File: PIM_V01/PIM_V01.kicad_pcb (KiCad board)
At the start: 2 copper layers, 95.9 x 90.2 mm, 10 parts, among them J1 Conn_02x30_Row_Letter_First, J2 Conn_02x30_Row_Letter_First

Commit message: a month of progress, schematic is nearly done (just needs to be checked), and layout is getting close'
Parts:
- removed H1, H2, H3, H4: MountingHole_Pad, MountingHole:MountingHole_3.2mm_M3_Pad_TopBottom
- removed H5, H6, H7, H8: MountingHole, MountingHole:MountingHole_2mm
- removed J2: Conn_02x30_Row_Letter_First, Connector_PinSocket_2.00mm:PinSocket_2x30_P2.00mm_Vertical
- added C1: 1uF, Capacitor_SMD:C_0603_1608Metric, F.Cu at (466.8, 68.0)
- added C10: 4.7uF, Capacitor_SMD:C_0603_1608Metric, F.Cu at (484.0, 103.5)
- added C100: 27pF, Capacitor_SMD:C_0603_1608Metric, F.Cu at (511.4, 136.0)
- added C101: 22uF, Capacitor_SMD:C_0603_1608Metric, F.Cu at (554.0, 70.8)
- added C102: 22uF, Capacitor_SMD:C_0603_1608Metric, F.Cu at (555.5, 70.8)
- added C11: 4.7uF, Capacitor_SMD:C_0603_1608Metric, F.Cu at (483.5, 115.5)
- added C12: 0.1uF, Capacitor_SMD:C_0603_1608Metric, F.Cu at (482.5, 103.5)
- added C13: 0.1uF, Capacitor_SMD:C_0603_1608Metric, F.Cu at (482.0, 115.5)
- added C14: 4.7uF, Capacitor_SMD:C_0603_1608Metric, F.Cu at (476.5, 99.2)
- added C15: 4.7uF, Capacitor_SMD:C_0603_1608Metric, F.Cu at (476.5, 111.2)
- added C16: 0.1uF, Capacitor_SMD:C_0603_1608Metric, F.Cu at (475.0, 99.2)
- added C17: 0.1uF, Capacitor_SMD:C_0603_1608Metric, F.Cu at (475.0, 111.2)
- added C18: 47pF, Capacitor_SMD:C_0603_1608Metric, F.Cu at (465.5, 102.0)
- added C19: 47pF, Capacitor_SMD:C_0603_1608Metric, F.Cu at (465.5, 114.0)
- added C2: 0.1uF, Capacitor_SMD:C_0603_1608Metric, F.Cu at (468.3, 68.0)
- added C20: 47pF, Capacitor_SMD:C_0603_1608Metric, F.Cu at (465.5, 105.0)
- added C21: 47pF, Capacitor_SMD:C_0603_1608Metric, F.Cu at (465.5, 117.0)
- added C22: 47pF, Capacitor_SMD:C_0603_1608Metric, F.Cu at (455.0, 102.0)
- added C23: 47pF, Capacitor_SMD:C_0603_1608Metric, F.Cu at (455.0, 114.0)
- added C24: 47pF, Capacitor_SMD:C_0603_1608Metric, F.Cu at (455.0, 105.0)
- added C25: 47pF, Capacitor_SMD:C_0603_1608Metric, F.Cu at (455.0, 117.0)
- added C26: 4.7nF, Capacitor_SMD:C_0603_1608Metric, F.Cu at (462.0, 106.5)
- added C27: 4.7nF, Capacitor_SMD:C_0603_1608Metric, F.Cu at (462.0, 118.5)
- added C28: 10uF, Capacitor_SMD:C_0603_1608Metric, F.Cu at (502.2, 67.1)
- added C29: 10uF, Capacitor_SMD:C_0603_1608Metric, F.Cu at (484.2, 67.2)
- added C3: 3.3nF, Capacitor_SMD:C_0603_1608Metric, F.Cu at (469.8, 63.4)
- added C30: 10uF, Capacitor_SMD:C_0603_1608Metric, F.Cu at (519.0, 67.0)
- added C31: 10uF, Capacitor_SMD:C_0603_1608Metric, F.Cu at (503.7, 67.1)
- added C32: 10uF, Capacitor_SMD:C_0603_1608Metric, F.Cu at (485.7, 67.2)
- added C33: 10uF, Capacitor_SMD:C_0603_1608Metric, F.Cu at (520.5, 67.0)
- added C34: 0.1uF, Capacitor_SMD:C_0603_1608Metric, F.Cu at (505.2, 67.1)
- added C35: 0.1uF, Capacitor_SMD:C_0603_1608Metric, F.Cu at (487.2, 67.2)
- added C36: 0.1uF, Capacitor_SMD:C_0603_1608Metric, F.Cu at (522.0, 67.0)
- added C37: 33nF, Capacitor_SMD:C_0603_1608Metric, F.Cu at (510.9, 65.0)
- added C38: 10nF, Capacitor_SMD:C_0603_1608Metric, F.Cu at (492.7, 65.1)
- added C39: 33nF, Capacitor_SMD:C_0603_1608Metric, F.Cu at (527.5, 65.0)
- added C4: 47uF, Capacitor_SMD:C_0603_1608Metric, F.Cu at (448.5, 67.5)
- added C40: 0.1uF, Capacitor_SMD:C_0603_1608Metric, F.Cu at (514.4, 66.5)
- added C41: 0.1uF, Capacitor_SMD:C_0603_1608Metric, F.Cu at (496.4, 66.6)
- added C42: 0.1uF, Capacitor_SMD:C_0603_1608Metric, F.Cu at (531.0, 66.5)
- added C43: 22uF, Capacitor_SMD:C_0603_1608Metric, F.Cu at (507.3, 79.1)
- added C44: 22uF, Capacitor_SMD:C_0603_1608Metric, F.Cu at (489.2, 79.1)
- added C45: 22uF, Capacitor_SMD:C_0603_1608Metric, F.Cu at (524.0, 78.8)
- added C46: 22uF, Capacitor_SMD:C_0603_1608Metric, F.Cu at (507.3, 80.6)
- added C47: 22uF, Capacitor_SMD:C_0603_1608Metric, F.Cu at (489.2, 80.6)
- added C48: 22uF, Capacitor_SMD:C_0603_1608Metric, F.Cu at (524.0, 80.3)
- added C49: 10uF, Capacitor_SMD:C_0603_1608Metric, F.Cu at (549.0, 93.9)
- added C5: 47uF, Capacitor_SMD:C_0603_1608Metric, F.Cu at (450.0, 67.5)
- added C50: 10uF, Capacitor_SMD:C_0603_1608Metric, F.Cu at (549.2, 111.0)
- added C51: 10uF, Capacitor_SMD:C_0603_1608Metric, F.Cu at (549.0, 92.4)
- added C52: 10uF, Capacitor_SMD:C_0603_1608Metric, F.Cu at (549.2, 109.5)
- added C53: 0.1uF, Capacitor_SMD:C_0603_1608Metric, F.Cu at (549.0, 90.9)
- added C54: 0.1uF, Capacitor_SMD:C_0603_1608Metric, F.Cu at (549.2, 108.0)
- added C55: 10nF, Capacitor_SMD:C_0603_1608Metric, F.Cu at (546.9, 85.4)
- added C56: 10nF, Capacitor_SMD:C_0603_1608Metric, F.Cu at (546.9, 102.3)
- added C57: 0.1uF, Capacitor_SMD:C_0603_1608Metric, F.Cu at (548.4, 82.0)
- added C58: 0.1uF, Capacitor_SMD:C_0603_1608Metric, F.Cu at (548.4, 98.8)
- added C59: 22uF, Capacitor_SMD:C_0603_1608Metric, F.Cu at (561.4, 89.1)
- added C6: 10uF, Capacitor_SMD:C_0603_1608Metric, F.Cu at (451.5, 67.5)
- added C60: 22uF, Capacitor_SMD:C_0603_1608Metric, F.Cu at (561.3, 106.0)
- added C61: 22uF, Capacitor_SMD:C_0603_1608Metric, F.Cu at (562.9, 89.1)
- added C62: 22uF, Capacitor_SMD:C_0603_1608Metric, F.Cu at (562.8, 106.0)
- added C63: 100nF, Capacitor_SMD:C_0603_1608Metric, F.Cu at (524.0, 100.5)
- added C64: 27pF, Capacitor_SMD:C_0603_1608Metric, F.Cu at (530.7, 141.0)
- added C65: 10nF, Capacitor_SMD:C_0603_1608Metric, F.Cu at (504.0, 64.3)
- added C66: 10nF, Capacitor_SMD:C_0603_1608Metric, F.Cu at (486.0, 64.5)
- added C67: 10nF, Capacitor_SMD:C_0603_1608Metric, F.Cu at (520.7, 64.4)
- added C68: 100uF, Capacitor_SMD:C_0603_1608Metric, F.Cu at (539.5, 71.1)
- added C69: 22uF, Capacitor_SMD:C_0603_1608Metric, F.Cu at (541.0, 71.1)
- added C7: 10uF, Capacitor_SMD:C_0603_1608Metric, F.Cu at (445.0, 86.7)
- added C70: 0.1uF, Capacitor_SMD:C_0603_1608Metric, F.Cu at (542.5, 71.1)
- added C71: 22nF, Capacitor_SMD:C_0603_1608Metric, F.Cu at (546.0, 76.6)
- added C72: 1uF, Capacitor_SMD:C_0603_1608Metric, F.Cu at (550.0, 73.6)
- added C73: 0.1uF, Capacitor_SMD:C_0603_1608Metric, F.Cu at (541.2, 67.4)
- added C74: 0.1uF, Capacitor_SMD:C_0603_1608Metric, F.Cu at (551.7, 67.4)
- added C75: 100uF, Capacitor_SMD:C_0603_1608Metric, F.Cu at (557.0, 70.8)
- added C76: 22uF, Capacitor_SMD:C_0603_1608Metric, F.Cu at (552.5, 70.8)
- added C77: 22uF, Capacitor_SMD:C_0603_1608Metric, F.Cu at (551.0, 70.8)
- added C78: 1uF, Capacitor_SMD:C_0603_1608Metric, F.Cu at (448.8, 80.2)
- added C79: 1uF, Capacitor_SMD:C_0603_1608Metric, F.Cu at (454.8, 80.2)
- added C8: 1uF, Capacitor_SMD:C_0603_1608Metric, F.Cu at (475.4, 68.3)
- added C80: 1uF, Capacitor_SMD:C_0603_1608Metric, F.Cu at (500.1, 86.3)
- added C81: 0.1uF, Capacitor_SMD:C_0603_1608Metric, F.Cu at (498.6, 86.3)
- added C82: 10uF, Capacitor_SMD:C_0603_1608Metric, F.Cu at (445.0, 80.3)
- added C83: 0.1uF, Capacitor_SMD:C_0603_1608Metric, F.Cu at (507.3, 77.6)
- added C84: 0.1uF, Capacitor_SMD:C_0603_1608Metric, F.Cu at (489.2, 77.6)
- added C85: 0.1uF, Capacitor_SMD:C_0603_1608Metric, F.Cu at (524.0, 77.3)
- added C86: 0.1uF, Capacitor_SMD:C_0603_1608Metric, F.Cu at (559.9, 89.1)
- added C87: 0.1uF, Capacitor_SMD:C_0603_1608Metric, F.Cu at (559.8, 106.0)
- added C88: 0.1uF, Capacitor_SMD:C_0603_1608Metric, F.Cu at (549.5, 70.8)
- added C89: 0.1uF, Capacitor_SMD:C_0603_1608Metric, F.Cu at (500.8, 108.0)
- added C9: 10uF, Capacitor_SMD:C_0603_1608Metric, F.Cu at (469.1, 79.5)
- added C90: 0.1uF, Capacitor_SMD:C_0603_1608Metric, F.Cu at (517.5, 111.0)
- added C91: 0.1uF, Capacitor_SMD:C_0603_1608Metric, F.Cu at (520.0, 105.4)
- added C92: 0.1uF, Capacitor_SMD:C_0603_1608Metric, F.Cu at (520.0, 102.3)
- added C93: 0.1uF, Capacitor_SMD:C_0603_1608Metric, F.Cu at (503.7, 91.5)
- added C94: 4.7uF, Capacitor_SMD:C_0603_1608Metric, F.Cu at (516.8, 91.3)
- added C95: 1uF, Capacitor_SMD:C_0603_1608Metric, F.Cu at (520.5, 96.5)
- added C96: 2.2uF, Capacitor_SMD:C_0603_1608Metric, F.Cu at (503.0, 88.5)
- added C97: 2.2uF, Capacitor_SMD:C_0603_1608Metric, F.Cu at (498.5, 106.3)
- added C98: 0.1uF, Capacitor_SMD:C_0603_1608Metric, F.Cu at (522.0, 96.5)
- added C99: 1uF, Capacitor_SMD:C_0603_1608Metric, F.Cu at (523.5, 96.5)
- added D1: SMBJ13A, CustomFootprints:SMBJ16A, F.Cu at (445.5, 67.5)
- added D10: LED, LED_SMD:LED_0603_1608Metric, F.Cu at (486.2, 82.1)
- added D11: LED, LED_SMD:LED_0603_1608Metric, F.Cu at (568.0, 86.4)
- added D12: LED, LED_SMD:LED_0603_1608Metric, F.Cu at (568.2, 102.9)
- added D13: SMAJ13A, Diode_SMD:D_SMA, F.Cu at (464.0, 65.9)
- added D2: LED, LED_SMD:LED_0603_1608Metric, F.Cu at (439.8, 91.5)
- added D3: PMEG4010, Diode_SMD:Nexperia_CFP3_SOD-123W, F.Cu at (473.5, 69.1)
- added D4: BZT52C15, Diode_SMD:Nexperia_CFP3_SOD-123W, F.Cu at (461.0, 66.5)
- added D5: D_TVS_Dual_AAC, Package_TO_SOT_SMD:SOT-23-3, F.Cu at (468.5, 115.5)
- added D6: D_TVS_Dual_AAC, Package_TO_SOT_SMD:SOT-23-3, F.Cu at (468.5, 103.5)
- added D7: D_TVS_Dual_AAC, Package_TO_SOT_SMD:SOT-23-3, F.Cu at (450.5, 103.5)
- added D8: D_TVS_Dual_AAC, Package_TO_SOT_SMD:SOT-23-3, F.Cu at (450.5, 115.5)
- added D9: LED, LED_SMD:LED_0603_1608Metric, F.Cu at (504.2, 82.2)
- added FL1: Choke_CommonMode_FerriteCore_1243, Inductor_SMD:L_CommonModeChoke_Coilcraft_1812CAN, F.Cu at (462.0, 103.5)
- added FL2: Choke_CommonMode_FerriteCore_1243, Inductor_SMD:L_CommonModeChoke_Coilcraft_1812CAN, F.Cu at (462.0, 115.5)
- added J10: Conn_02x08_Odd_Even, Connector_PinHeader_2.54mm:PinHeader_2x08_P2.54mm_Vertical, F.Cu at (525.7, 123.0)
- added J11: Conn_01x02, Connector_PinHeader_2.54mm:PinHeader_1x02_P2.54mm_Vertical, F.Cu at (563.7, 83.3)
- added J12: Conn_01x02, Connector_PinHeader_2.54mm:PinHeader_1x02_P2.54mm_Vertical, F.Cu at (563.9, 100.0)
- added J13: Conn_01x02, Connector_PinHeader_2.54mm:PinHeader_1x02_P2.54mm_Vertical, F.Cu at (563.7, 70.3)
- added J4: USB_C_Receptacle_USB2.0_14P, Connector_USB:USB_C_Receptacle_HCTL_HC-TYPE-C-16P-01A, F.Cu at (439.3, 83.5)
- added J5: Conn_01x04, Connector_Molex:Molex_PicoBlade_53261-0471_1x04-1MP_P1.25mm_Horizontal, F.Cu at (438.5, 103.5)
- added J6: Conn_01x04, Connector_Molex:Molex_PicoBlade_53261-0471_1x04-1MP_P1.25mm_Horizontal, F.Cu at (438.5, 115.5)
- added J7: Conn_02x03_Odd_Even, Connector_PinHeader_2.54mm:PinHeader_2x03_P2.54mm_Vertical, F.Cu at (495.0, 115.3)
- added J8: Conn_01x02, Connector_PinHeader_2.54mm:PinHeader_1x02_P2.54mm_Vertical, F.Cu at (513.5, 118.0)
- added J9: Conn_02x08_Odd_Even, Connector_PinHeader_2.54mm:PinHeader_2x08_P2.54mm_Vertical, F.Cu at (504.0, 123.0)
- added L1: 6.8uH, CustomFootprints:L_Wurth_WE-LHMI-7030, F.Cu at (511.0, 72.4)
- added L2: 6.8uH, CustomFootprints:L_Wurth_WE-LHMI-7030, F.Cu at (492.5, 72.4)
- added L3: 6.8uH, CustomFootprints:L_Wurth_WE-LHMI-7030, F.Cu at (527.0, 72.0)
- added L4: 6.8uH, CustomFootprints:L_Wurth_WE-LHMI-7030, F.Cu at (554.0, 85.4)
- added L5: 6.8uH, CustomFootprints:L_Wurth_WE-LHMI-7030, F.Cu at (554.0, 102.5)
- added L6: 4.7uH, CustomFootprints:L_Wurth_WE-LHMI-7050, F.Cu at (546.5, 63.5)
- added Q1: SQJ407EP-T1_GE3, CustomFootprints:PowerPAK-SO-8L_Option-2_VIS, F.Cu at (456.0, 67.5)
- added Q2: PMOS, Package_TO_SOT_SMD:SOT-23-3, F.Cu at (472.1, 77.5)
- added Q3: PMOS, Package_TO_SOT_SMD:SOT-23-3, F.Cu at (472.1, 81.5)
- added Q4: NMOS, Package_TO_SOT_SMD:SOT-23-3, F.Cu at (472.1, 73.5)
- added R1: 5k1R, Resistor_SMD:R_0603_1608Metric, F.Cu at (442.7, 77.3)
- added R10: 0R, Resistor_SMD:R_0603_1608Metric, F.Cu at (549.5, 68.1)
- added R11: 0R, Resistor_SMD:R_0603_1608Metric, F.Cu at (475.1, 79.2)
- added R12: 1MR, Resistor_SMD:R_0603_1608Metric, F.Cu at (476.6, 79.2)
- added R13: 10kR, Resistor_SMD:R_0603_1608Metric, F.Cu at (512.7, 115.4)
- added R14: 10kR, Resistor_SMD:R_0603_1608Metric, F.Cu at (475.8, 109.0)
- added R15: 10kR, Resistor_SMD:R_0603_1608Metric, F.Cu at (476.0, 121.0)
- added R16: 0R, Resistor_SMD:R_0603_1608Metric, F.Cu at (475.8, 107.5)
- added R17: 0R, Resistor_SMD:R_0603_1608Metric, F.Cu at (476.0, 119.5)
- added R18: 60R, Resistor_SMD:R_0603_1608Metric, F.Cu at (453.5, 105.0)
- added R19: 60R, Resistor_SMD:R_0603_1608Metric, F.Cu at (453.5, 102.0)
- added R2: 866kR, Resistor_SMD:R_0603_1608Metric, F.Cu at (467.5, 65.7)
- added R20: 60R, Resistor_SMD:R_0603_1608Metric, F.Cu at (453.5, 117.0)
- added R21: 60R, Resistor_SMD:R_0603_1608Metric, F.Cu at (453.5, 114.0)
- added R22: 0R, Resistor_SMD:R_0603_1608Metric, F.Cu at (506.7, 62.0)
- added R23: 0R, Resistor_SMD:R_0603_1608Metric, F.Cu at (488.7, 62.2)
- added R24: 0R, Resistor_SMD:R_0603_1608Metric, F.Cu at (523.5, 62.0)
- added R25: 52.3kR, Resistor_SMD:R_0603_1608Metric, F.Cu at (510.4, 62.0)
- added R26: 10kR, Resistor_SMD:R_0603_1608Metric, F.Cu at (508.8, 62.0)
- added R27: 31.6kR, Resistor_SMD:R_0603_1608Metric, F.Cu at (492.2, 62.2)
- added R28: 10kR, Resistor_SMD:R_0603_1608Metric, F.Cu at (490.7, 62.2)
- added R29: 4.99kR, Resistor_SMD:R_0603_1608Metric, F.Cu at (527.0, 62.0)
- added R3: 150kR, Resistor_SMD:R_0603_1608Metric, F.Cu at (467.5, 64.2)
- added R30: 10kR, Resistor_SMD:R_0603_1608Metric, F.Cu at (525.5, 62.0)
- added R31: 470R, Resistor_SMD:R_0603_1608Metric, F.Cu at (507.2, 82.2)
- added R32: 470R, Resistor_SMD:R_0603_1608Metric, F.Cu at (489.2, 82.1)
- added R33: 470R, Resistor_SMD:R_0603_1608Metric, F.Cu at (565.0, 86.4)
- added R34: 470R, Resistor_SMD:R_0603_1608Metric, F.Cu at (565.2, 102.9)
- added R35: 0R, Resistor_SMD:R_0603_1608Metric, F.Cu at (544.0, 89.7)
- added R36: 0R, Resistor_SMD:R_0603_1608Metric, F.Cu at (544.0, 106.5)
- added R37: 52.3kR, Resistor_SMD:R_0603_1608Metric, F.Cu at (544.0, 86.1)
- added R38: 10kR, Resistor_SMD:R_0603_1608Metric, F.Cu at (544.0, 87.6)
- added R39: 31.6kR, Resistor_SMD:R_0603_1608Metric, F.Cu at (544.0, 103.0)
- added R4: 5k1R, Resistor_SMD:R_0603_1608Metric, F.Cu at (442.7, 89.7)
- added R40: 10kR, Resistor_SMD:R_0603_1608Metric, F.Cu at (544.0, 104.5)
- added R41: 1kR, Resistor_SMD:R_0603_1608Metric, F.Cu at (480.0, 111.2)
- added R42: 1kR, Resistor_SMD:R_0603_1608Metric, F.Cu at (480.0, 119.9)
- added R43: 1kR, Resistor_SMD:R_0603_1608Metric, F.Cu at (480.0, 108.0)
- added R44: 1kR, Resistor_SMD:R_0603_1608Metric, F.Cu at (480.0, 99.0)
- added R45: 470kR, Resistor_SMD:R_0603_1608Metric, F.Cu at (503.2, 62.0)
- added R46: 100kR, Resistor_SMD:R_0603_1608Metric, F.Cu at (504.7, 62.0)
- added R47: 470kR, Resistor_SMD:R_0603_1608Metric, F.Cu at (485.2, 62.2)
- added R48: 100kR, Resistor_SMD:R_0603_1608Metric, F.Cu at (486.7, 62.2)
- added R49: 470kR, Resistor_SMD:R_0603_1608Metric, F.Cu at (520.0, 62.0)
- added R5: 511R, Resistor_SMD:R_0603_1608Metric, F.Cu at (474.5, 64.4)
- added R50: 100kR, Resistor_SMD:R_0603_1608Metric, F.Cu at (521.5, 62.0)
- added R51: 4.7kR, Resistor_SMD:R_0603_1608Metric, F.Cu at (513.0, 113.0)
- added R52: 4.7kR, Resistor_SMD:R_0603_1608Metric, F.Cu at (511.5, 113.0)
- added R53: 430kR, Resistor_SMD:R_0603_1608Metric, F.Cu at (550.0, 76.6)
- added R54: 400kR, Resistor_SMD:R_0603_1608Metric, F.Cu at (550.0, 75.1)
- added R55: 21.5kR, Resistor_SMD:R_0603_1608Metric, F.Cu at (544.5, 76.6)
- added R56: 43.2kR, Resistor_SMD:R_0603_1608Metric, F.Cu at (550.0, 78.1)
- added R57: 4.7kR, Resistor_SMD:R_0603_1608Metric, F.Cu at (507.0, 87.0)
- added R58: 4.7kR, Resistor_SMD:R_0603_1608Metric, F.Cu at (505.5, 87.0)
- added R59: 10kR, Resistor_SMD:R_0603_1608Metric, F.Cu at (506.0, 112.7)
- added R6: 470R, Resistor_SMD:R_0603_1608Metric, F.Cu at (442.8, 91.5)
- added R60: 10kR, Resistor_SMD:R_0603_1608Metric, F.Cu at (511.0, 87.0)
- added R61: 10kR, Resistor_SMD:R_0603_1608Metric, F.Cu at (509.5, 87.0)
- added R62: 33R, Resistor_SMD:R_0603_1608Metric, F.Cu at (515.5, 86.5)
- added R63: 33R, Resistor_SMD:R_0603_1608Metric, F.Cu at (513.5, 86.5)
- added R64: 33R, Resistor_SMD:R_0603_1608Metric, F.Cu at (497.5, 98.0)
- added R65: 33R, Resistor_SMD:R_0603_1608Metric, F.Cu at (497.5, 99.5)
- added R66: 10kR, Resistor_SMD:R_0603_1608Metric, F.Cu at (494.5, 98.0)
- added R67: 10kR, Resistor_SMD:R_0603_1608Metric, F.Cu at (497.5, 101.0)
- added R68: 100kR, Resistor_SMD:R_0603_1608Metric, F.Cu at (476.6, 73.4)
- added R69: 1MR, Resistor_SMD:R_0603_1608Metric, F.Cu at (475.1, 73.4)
- added R7: 10kR, Resistor_SMD:R_0603_1608Metric, F.Cu at (474.5, 65.9)
- added R70: 100kR, Resistor_SMD:R_0603_1608Metric, F.Cu at (469.1, 75.5)
- added R71: 100kR, Resistor_SMD:R_0603_1608Metric, F.Cu at (546.4, 109.3)
- added R72: 100kR, Resistor_SMD:R_0603_1608Metric, F.Cu at (546.0, 92.9)
- added R73: 100kR, Resistor_SMD:R_0603_1608Metric, F.Cu at (541.7, 74.0)
- added R74: 0R, Resistor_SMD:R_0603_1608Metric, F.Cu at (528.0, 66.5)
- added R75: 0R, Resistor_SMD:R_0603_1608Metric, F.Cu at (493.3, 66.6)
- added R76: 0R, Resistor_SMD:R_0603_1608Metric, F.Cu at (511.4, 66.5)
- added R77: 0R, Resistor_SMD:R_0603_1608Metric, F.Cu at (548.4, 85.0)
- added R78: 0R, Resistor_SMD:R_0603_1608Metric, F.Cu at (548.4, 101.8)
- added R8: 100kR, Resistor_SMD:R_0603_1608Metric, F.Cu at (461.0, 62.5)
- added R9: 0R, Resistor_SMD:R_0603_1608Metric, F.Cu at (543.5, 68.1)
- added SW1: SW_Push, Button_Switch_SMD:SW_SPST_B3U-1000P, F.Cu at (541.5, 138.5)
- added TP1: TestPoint, TestPoint:TestPoint_Keystone_5000-5004_Miniature, F.Cu at (471.5, 105.5)
- added TP2: TestPoint, TestPoint:TestPoint_Keystone_5000-5004_Miniature, F.Cu at (471.5, 101.5)
- added TP3: TestPoint, TestPoint:TestPoint_Keystone_5000-5004_Miniature, F.Cu at (471.5, 117.5)
- added TP4: TestPoint, TestPoint:TestPoint_Keystone_5000-5004_Miniature, F.Cu at (471.5, 113.5)
- added TP5: TestPoint, TestPoint:TestPoint_Keystone_5000-5004_Miniature, F.Cu at (457.5, 105.5)
- added TP6: TestPoint, TestPoint:TestPoint_Keystone_5000-5004_Miniature, F.Cu at (457.5, 101.5)
- added TP7: TestPoint, TestPoint:TestPoint_Keystone_5000-5004_Miniature, F.Cu at (457.5, 117.5)
- added TP8: TestPoint, TestPoint:TestPoint_Keystone_5000-5004_Miniature, F.Cu at (457.5, 113.5)
- added U1: TPS259541DSGR, CustomFootprints:DSG0008A, F.Cu at (470.7, 66.6)
- added U10: TPS62933, Package_TO_SOT_SMD:SOT-583-8, F.Cu at (547.7, 105.5)
- added U11: AP2112K-3.3, Package_TO_SOT_SMD:SOT-23-5, F.Cu at (451.8, 80.2)
- added U12: MP28167GQ-A-P, CustomFootprints:QFN-16_MP28167_MNP, F.Cu at (546.5, 71.6)
- added U13: MT29F1G01ABAFDWB-IT_F, Package_SON:WSON-8-1EP_8x6mm_P1.27mm_EP3.4x4.3mm, F.Cu at (493.2, 89.0)
- added U14: MB85RS256B, Package_SO:JEITA_SOIC-8_3.9x4.9mm_P1.27mm, F.Cu at (524.5, 143.1)
- added U2: USBLC6-2SC6, Package_TO_SOT_SMD:SOT-23-6, F.Cu at (448.7, 83.5)
- added U3: STM32H7A3VITx, Package_QFP:LQFP-100_14x14mm_P0.5mm, F.Cu at (510.5, 101.0)
- added U4: MCP2562FDT-E/SN, Package_SO:SOIC-8_3.9x4.9mm_P1.27mm, F.Cu at (477.5, 103.5)
- added U5: MCP2562FDT-E/SN, Package_SO:SOIC-8_3.9x4.9mm_P1.27mm, F.Cu at (477.5, 115.5)
- added U6: TPS62933, Package_TO_SOT_SMD:SOT-583-8, F.Cu at (507.8, 65.6)
- added U7: TPS62933, Package_TO_SOT_SMD:SOT-583-8, F.Cu at (489.7, 65.7)
- added U8: TPS62933, Package_TO_SOT_SMD:SOT-583-8, F.Cu at (524.5, 65.5)
- added U9: TPS62933, Package_TO_SOT_SMD:SOT-583-8, F.Cu at (547.5, 88.6)
- added Y1: Crystal_GND24_Small, Crystal:Crystal_SMD_Abracon_ABM8G-4Pin_3.2x2.5mm, F.Cu at (504.0, 139.5)
- J1: value Conn_02x30_Row_Letter_First -> Conn_01x06; footprint Connector_PinSocket_2.00mm:PinSocket_2x30_P2.00mm_Vertical -> Connector_Molex:Molex_Pico-Lock_504050-0691_1x06-1MP_P1.50mm_Horizontal
- moved J1 384.0 mm to (439.0, 67.5), turned to -90 degrees
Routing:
- net /OCTOSPI1_BK2_IO2: track 0.00 -> 40.8 mm
- net /CAN1_TX: track 0.00 -> 39.1 mm, vias 0 -> 2
- net +3V3_HK: track 0.00 -> 37.5 mm, vias 0 -> 8
- net +3V3_MCU: track 0.00 -> 35.9 mm, vias 0 -> 14
- net +5V_HK: track 0.00 -> 30.5 mm, vias 0 -> 6
- net /CAN1_RX: track 0.00 -> 28.9 mm, vias 0 -> 2
- net /OCTOSPI1_BK2_IO1: track 0.00 -> 26.6 mm, vias 0 -> 2
- net Net-(C27-Pad1): track 0.00 -> 26.5 mm
- net Net-(C26-Pad1): track 0.00 -> 26.5 mm
- net +5V_USB: track 0.00 -> 22.2 mm, vias 0 -> 10
- net /OCTOSPI1_BK2_IO3: track 0.00 -> 20.0 mm
- net /OCTOSPI1_CLK: track 0.00 -> 18.3 mm, vias 0 -> 3
- net /OCTOSPI1_BK2_IO0: track 0.00 -> 17.9 mm, vias 0 -> 2
- net +3V3_PL: track 0.00 -> 17.2 mm
- net +1V2_HK: track 0.00 -> 16.9 mm
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- added copper zone on F.Cu, net (none)
- added copper zone on F.Cu, net +12V_HK
- added copper zone on In2.Cu, net +12V_HK
- added copper zone on F.Cu, net +12V_IN
- added copper zone on F.Cu, net +12V_PL
- added copper zone on F.Cu, net +1V2_HK
- added copper zone on F.Cu, net +3V3_HK
- added copper zone on In2.Cu, net +3V3_HK
- added copper zone on F.Cu, net +3V3_MCU
- added copper zone on F.Cu, net +3V3_PL
- added copper zone on In2.Cu, net +5V_HK
- added copper zone on F.Cu, net +5V_PL
- added copper zone on In2.Cu, net +5V_USB
- added copper zone on F.Cu, net +VARI_PL
- added copper zone on In2.Cu, net +VARI_PL
- added copper zone on F.Cu, net Net-(U12-SW1)
- added copper zone on F.Cu, net Net-(U12-SW2)
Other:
- board size 95.9 x 90.2 mm -> 135.5 x 69 mm
- copper layers 2 -> 4
- board text added: "(ensure shared)"
- board text added: "+3V3"
- board text added: "+5V"
- board text added: "+5V_IN"
- board text added: "C1"
- board text added: "C10"
- board text added: "C11"
- board text added: "C12"
- board text added: "C13"
- board text added: "C14"
- board text added: "C15"
- board text added: "C16"
- board text added: "C17"
- board text added: "C18"
- board text added: "C19"
- board text added: "C2"
- board text added: "C20"
- board text added: "C3"
- board text added: "C4"
- board text added: "C5"
- board text added: "C6"
- board text added: "C7"
- board text added: "C8"
- board text added: "C9"
- board text added: "CAN Breakout V01"
- board text added: "CAN0_FILT_N"
- board text added: "CAN0_FILT_P"
- board text added: "CAN0_N"
- board text added: "CAN0_P"
- board text added: "CAN0_RAW_N"
- board text added: "CAN0_RAW_P"
- board text added: "CAN1_FILT_N"
- board text added: "CAN1_FILT_P"
- board text added: "CAN1_N"
- board text added: "CAN1_P"
- board text added: "CAN1_RAW_N"
- board text added: "CAN1_RAW_P"
- board text added: "D2"
- board text added: "D3"
- board text added: "D4"
- board text added: "D5"
- board text added: "D6"
- board text added: "FL1"
- board text added: "FL2"
- board text added: "GND"
- board text added: "J1"
- board text added: "J10"
- board text added: "J2"
- board text added: "J3"
- board text added: "J4"
- board text added: "J5"
- board text added: "J6"
- board text added: "J7"
- board text added: "J8"
- board text added: "J9"
- board text added: "Kala Payinda"
- board text added: "Q1"
- board text added: "R1"
- board text added: "R10"
- board text added: "R11"
- board text added: "R2"
- board text added: "R3"
- board text added: "R4"
- board text added: "R5"
- board text added: "R6"
- board text added: "R7"
- board text added: "R8"
- board text added: "R9"
- board text added: "RXD0"
- board text added: "RXD1"
- board text added: "STBY_0"
- board text added: "STBY_1"
- board text added: "TP1"
- board text added: "TP10"
- board text added: "TP11"
- board text added: "TP12"
- board text added: "TP13"
- board text added: "TP14"
- board text added: "TP15"
- board text added: "TP2"
- board text added: "TP3"
- board text added: "TP5"
- board text added: "TP8"
- board text added: "TP9"
- board text added: "TXD0"
- board text added: "TXD1"
- board text added: "U1"
- board text added: "U2"
- board text added: "U3"
- board text removed: "A1"
- board text removed: "A30"
- board text removed: "B"
- board text removed: "C"
- board text removed: "D30"

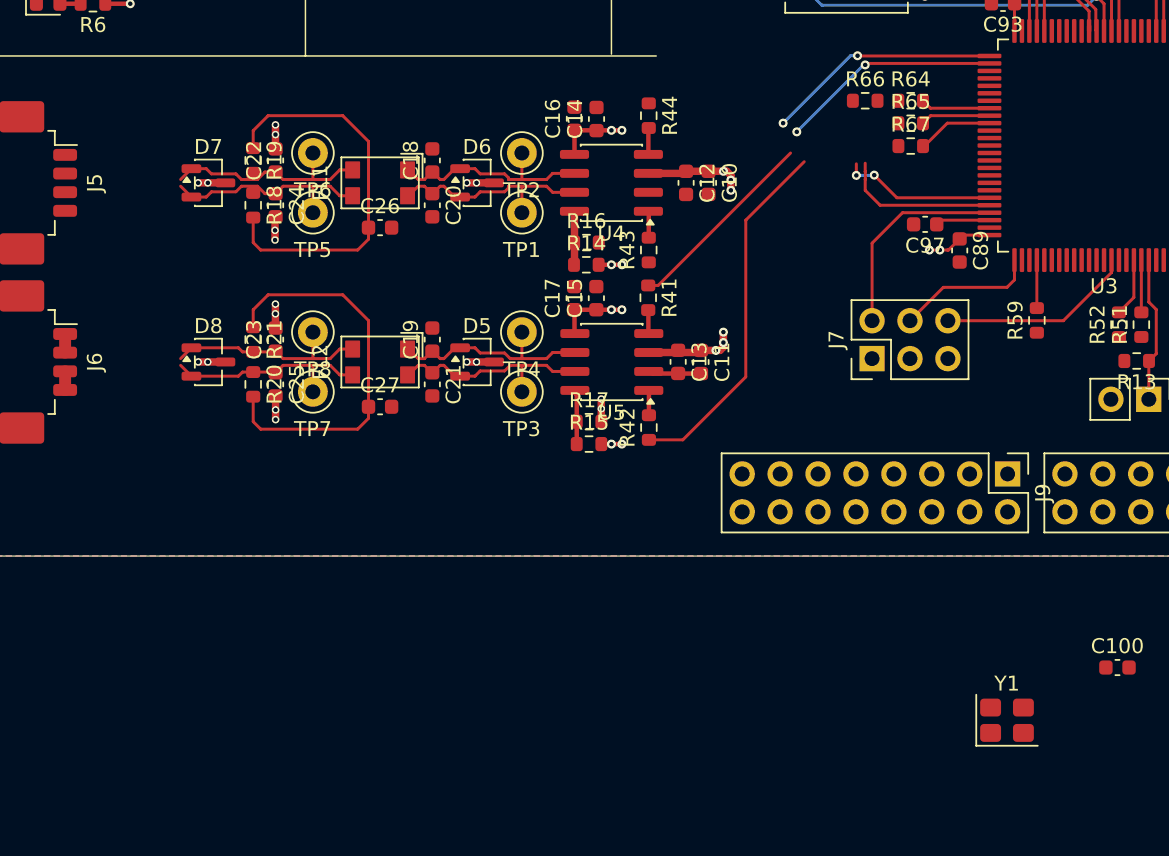
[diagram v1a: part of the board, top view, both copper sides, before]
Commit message: updated schematic to include FRAM. Ben to review soon'
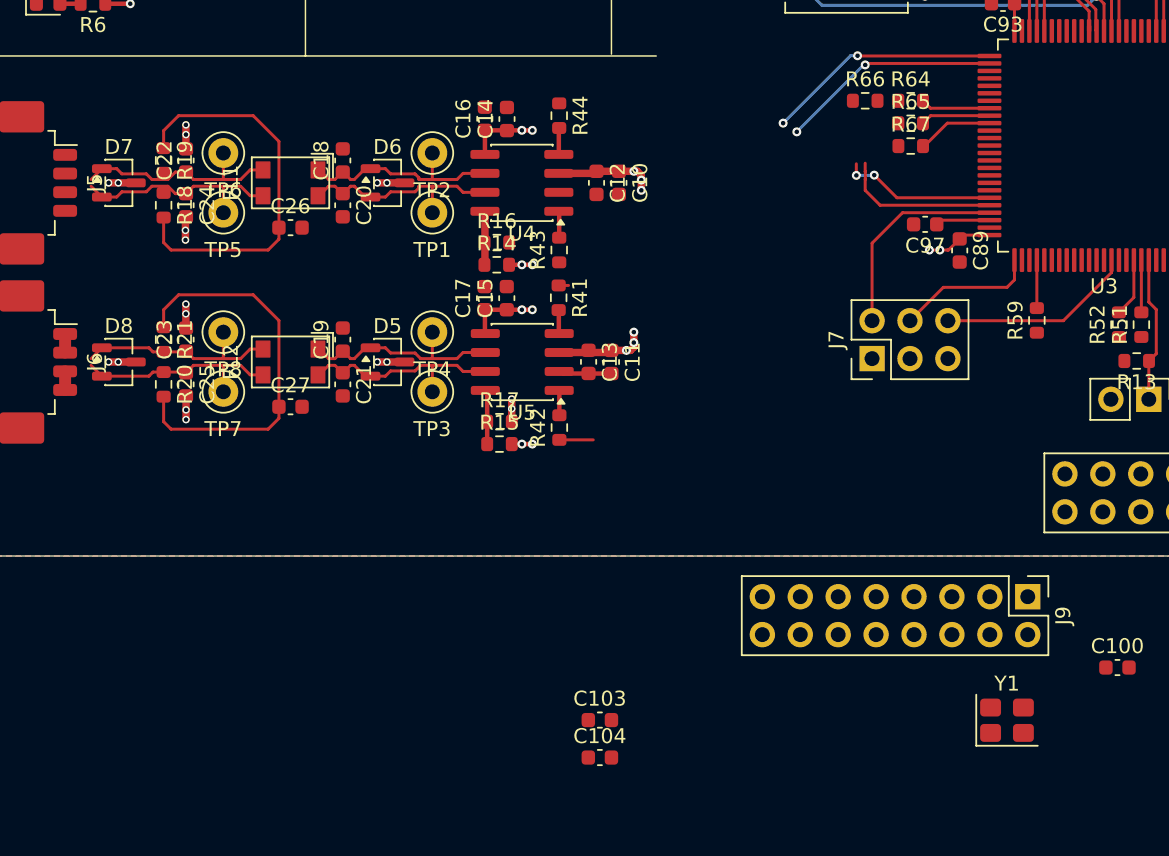
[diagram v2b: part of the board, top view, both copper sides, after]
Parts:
- added C103: 0.1uF, Capacitor_SMD:C_0603_1608Metric, F.Cu at (476.7, 139.5)
- added C104: 1uF, Capacitor_SMD:C_0603_1608Metric, F.Cu at (476.7, 142.0)
- moved J9 8.34 mm to (505.4, 131.2)
- moved C10 6.00 mm to (478.0, 103.5)
- moved C11 6.00 mm to (477.5, 115.5)
- moved C12 6.00 mm to (476.5, 103.5)
- moved C13 6.00 mm to (476.0, 115.5)
- moved C14 6.00 mm to (470.5, 99.2)
- moved C15 6.00 mm to (470.5, 111.2)
- moved C16 6.00 mm to (469.0, 99.2)
- moved C17 6.00 mm to (469.0, 111.2)
- moved C18 6.00 mm to (459.5, 102.0)
- moved C19 6.00 mm to (459.5, 114.0)
- moved C20 6.00 mm to (459.5, 105.0)
- moved C21 6.00 mm to (459.5, 117.0)
- moved C22 6.00 mm to (449.0, 102.0)
- moved C23 6.00 mm to (449.0, 114.0)
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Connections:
- J10 pad 11: unconnected-(J10-Pin_11-Pad11) -> /SPI2_MISO_PL
- J10 pad 13: unconnected-(J10-Pin_13-Pad13) -> /SPI2_MOSI_PL
- J10 pad 15: unconnected-(J10-Pin_15-Pad15) -> /SPI2_nCS_PL
- J10 pad 2: +3V3_MCU -> GND
- J10 pad 9: unconnected-(J10-Pin_9-Pad9) -> /SPI2_SCK_PL
- U14 pad 3: unconnected-(U14-~{WP}-Pad3) -> +3V3_MCU
- U14 pad 7: unconnected-(U14-~{HOLD}-Pad7) -> +3V3_MCU
- U3 pad 45: /SPI4_NSS_FRAM -> /SPI4_nSS_FRAM
- U3 pad 53: unconnected-(U3-PB14-Pad53) -> /SPI2_MISO_PL
- U3 pad 54: unconnected-(U3-PB15-Pad54) -> /SPI2_MOSI_PL
- U3 pad 85: unconnected-(U3-PD4-Pad85) -> /SPI2_nCS_PL
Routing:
- net /CAN1_TX: track 39.1 -> 17.1 mm
- net /CAN1_RX: track 28.9 -> 16.4 mm

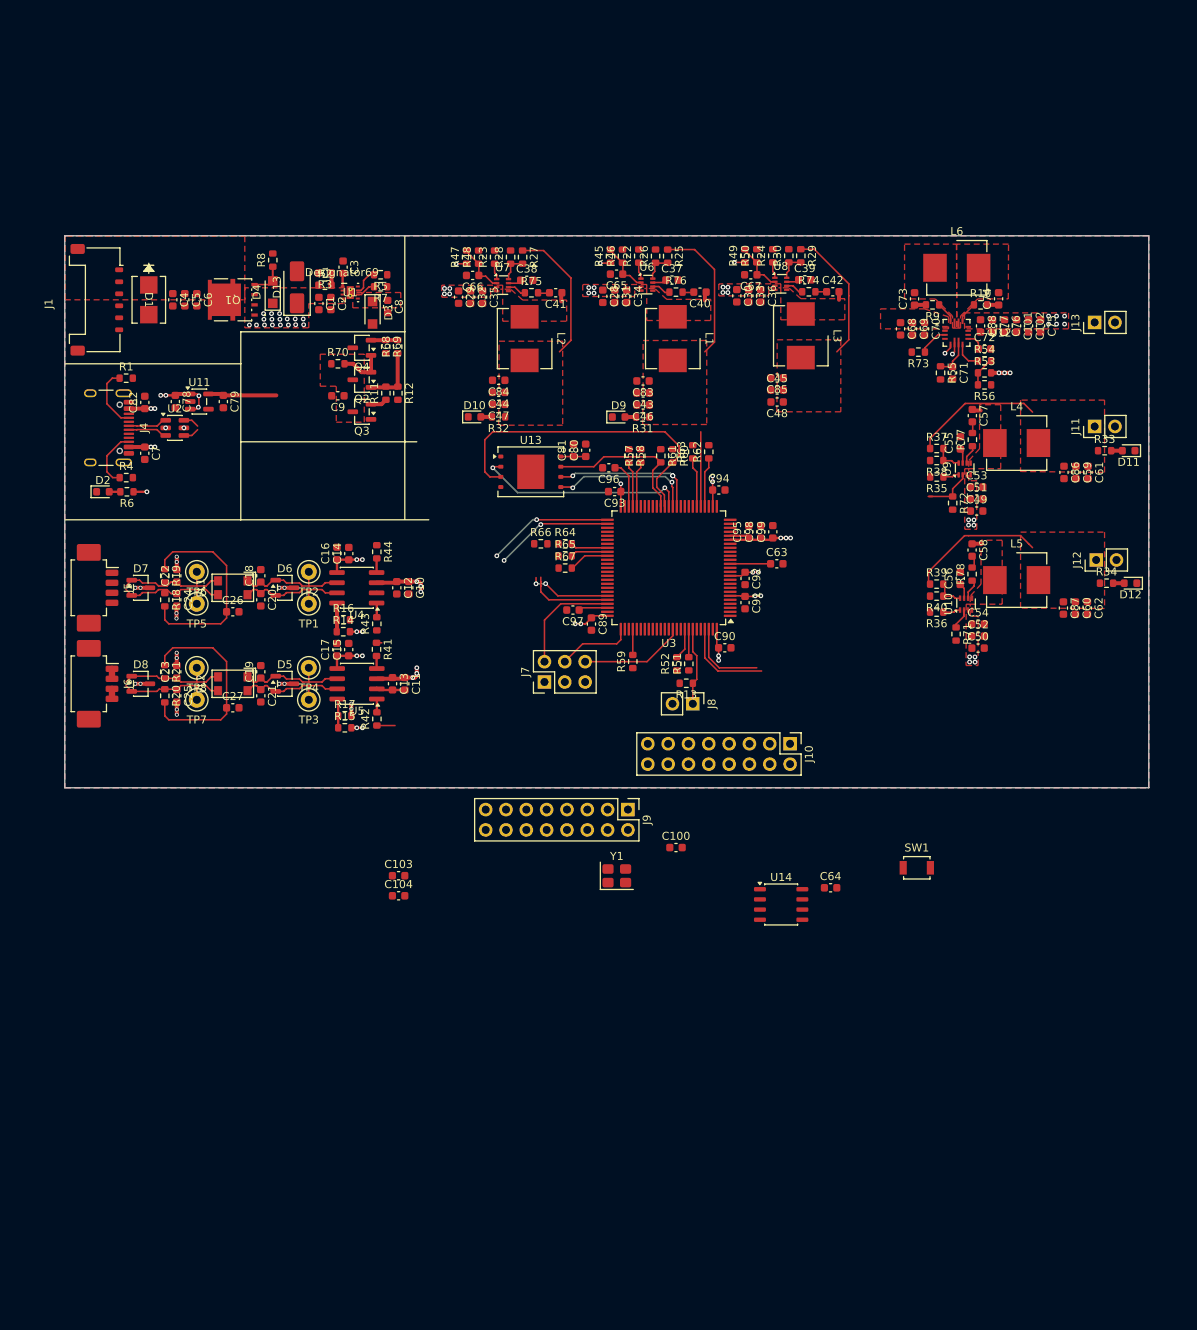
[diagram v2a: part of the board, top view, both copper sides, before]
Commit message: minor updates to sch, bigger updates to pcb, after this push i am moving to double sided pcb for space optimisation
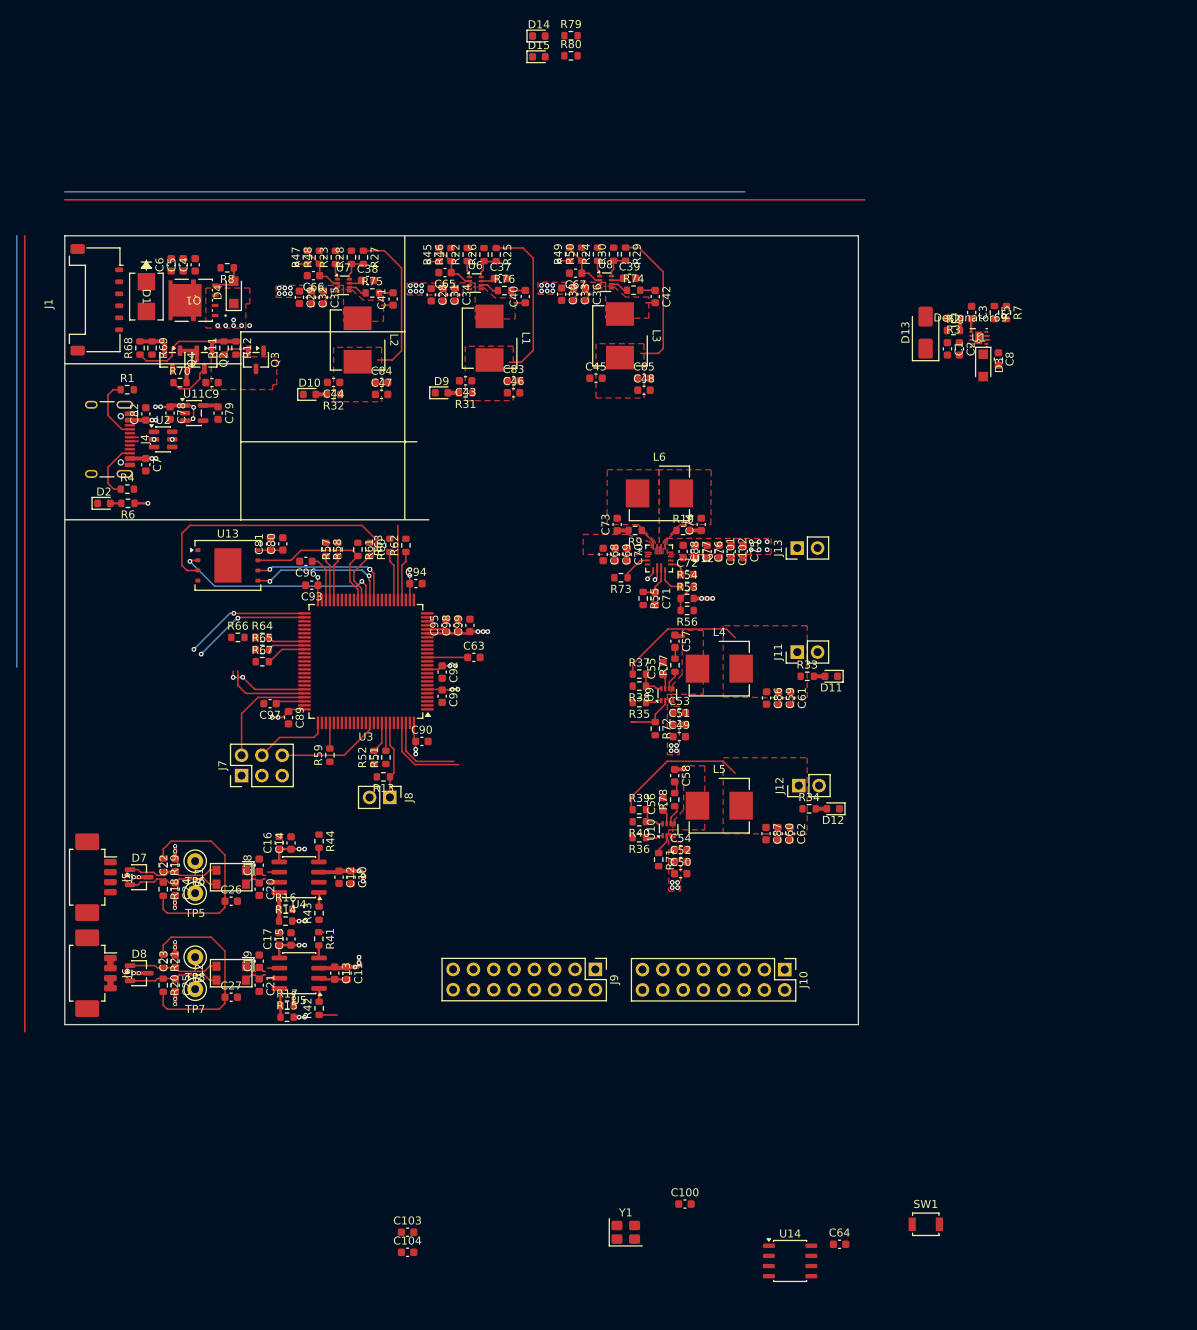
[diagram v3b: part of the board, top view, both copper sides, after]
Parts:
- removed D5, D6: D_TVS_Dual_AAC, Package_TO_SOT_SMD:SOT-23-3
- removed TP1, TP2, TP3, TP4: TestPoint, TestPoint:TestPoint_Keystone_5000-5004_Miniature
- added D14: LED, LED_SMD:LED_0603_1608Metric, F.Cu at (494.3, 34.5)
- added D15: LED, LED_SMD:LED_0603_1608Metric, F.Cu at (494.3, 37.1)
- added R79: 1.8kR, Resistor_SMD:R_0603_1608Metric, F.Cu at (498.3, 34.5)
- added R80: 1.8kR, Resistor_SMD:R_0603_1608Metric, F.Cu at (498.3, 37.0)
- R32, R34: value 470R -> 100R
- moved D13 78.8 mm to (542.6, 71.6)
- moved U1 78.8 mm to (549.2, 72.3)
- moved C1 78.8 mm to (545.3, 73.6)
- moved C2 78.8 mm to (546.8, 73.6)
- moved C3 78.8 mm to (548.4, 69.1)
- moved R2 78.8 mm to (546.1, 71.3)
- moved R3 78.8 mm to (546.1, 69.8)
- moved R7 78.3 mm to (552.7, 69.1), turned to -90 degrees
- moved R5 76.9 mm to (551.2, 69.1), turned to -90 degrees
- moved C8 76.6 mm to (551.7, 74.9)
- moved D3 76.6 mm to (549.8, 75.7)
- moved C74 46.7 mm to (514.6, 95.6)
- moved J11 46.7 mm to (526.6, 111.5)
- moved J13 46.7 mm to (526.6, 98.5)
- moved R73 46.7 mm to (504.5, 102.2)
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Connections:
- R73 pad 1: /POWER/+VARI_EN -> /+VARI_EN
- U12 pad 3: /POWER/+VARI_EN -> /+VARI_EN
- U3 pad 57: /PAYLOAD_nEN -> unconnected-(U3-PD10-Pad57)
- U3 pad 68: /USB_VBUS_SEN -> unconnected-(U3-PA9-Pad68)
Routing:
- net /CAN/CAN0_RAW_P: track 14.5 -> 4.58 mm
- net /CAN/CAN0_RAW_N: track 14.5 -> 4.58 mm
- net /CAN/CAN1_RAW_P: track 14.4 -> 4.58 mm
- net /CAN/CAN1_RAW_N: track 14.4 -> 4.58 mm
- net +3V3_HK: track 37.5 -> 47.3 mm
- net +3V3_USB: track 8.56 -> 1.93 mm
- net +3V3_MCU: track 35.9 -> 41.5 mm
- net /+VARI_EN: track 0.00 -> 3.72 mm
- net /POWER/+VARI_EN: track 3.72 -> 0.00 mm
- net /D-: track 4.92 -> 1.36 mm
- net /D+: track 4.91 -> 1.36 mm
- net Net-(U1-ILM): track 3.37 -> 0.37 mm
- net GND: track 16.3 -> 13.5 mm, vias 19 -> 15
- net +5V_HK: track 30.5 -> 33.1 mm
- net /USB_D-: track 12.4 -> 10.3 mm
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- added copper zone on F.Cu, net Net-(U6-SW)
- added copper zone on F.Cu, net Net-(U7-SW)
- added copper zone on F.Cu, net Net-(U8-SW)
- removed copper zone on F.Cu, net +12V_IN
- removed copper zone on B.Cu, net GND
- removed copper zone on F.Cu, net GND
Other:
- board size 135.5 x 69 mm -> 99.2 x 98.6 mm
